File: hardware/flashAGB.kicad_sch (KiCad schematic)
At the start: 1 part

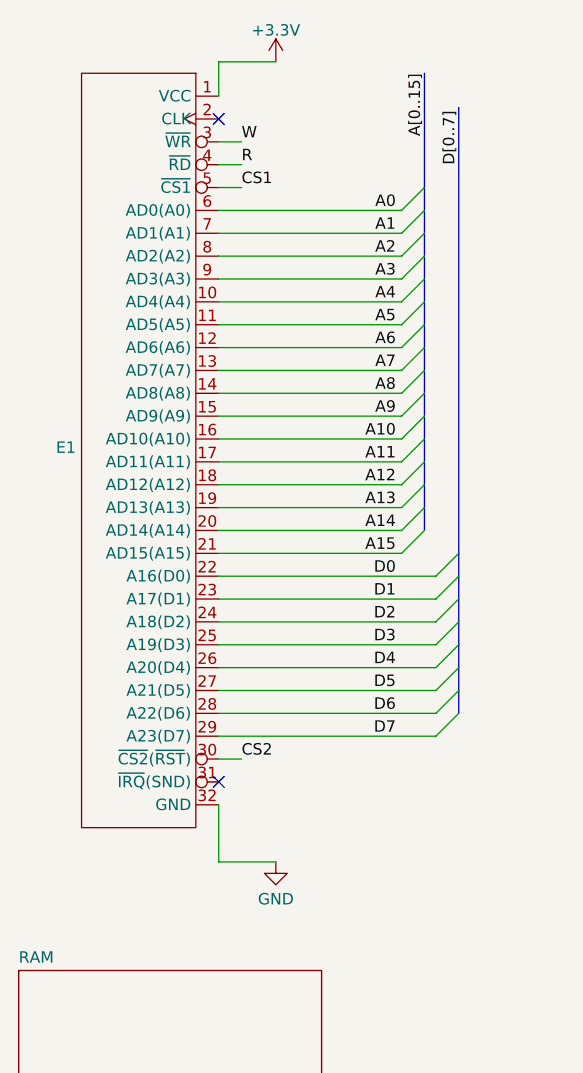
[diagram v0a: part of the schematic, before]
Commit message: Added feRAM
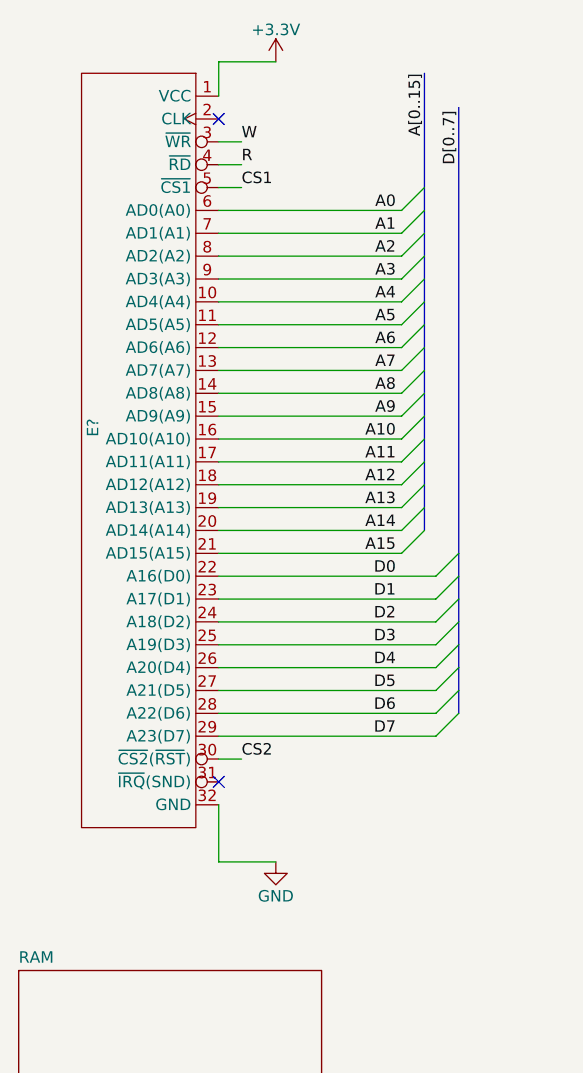
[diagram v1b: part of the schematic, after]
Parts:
- removed E1: ~, symbol AGB_cart:Cart
- added E?: ~, symbol AGB_common:Cart
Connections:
- net +3.3V: now also E?.1 (VCC)
- net A0: now also E?.6 (AD0(A0))
- net A1: now also E?.7 (AD1(A1))
- net A10: now also E?.16 (AD10(A10))
- net A11: now also E?.17 (AD11(A11))
- net A12: now also E?.18 (AD12(A12))
- net A13: now also E?.19 (AD13(A13))
- net A14: now also E?.20 (AD14(A14))
- net A15: now also E?.21 (AD15(A15))
- net A2: now also E?.8 (AD2(A2))
- net A3: now also E?.9 (AD3(A3))
- net A4: now also E?.10 (AD4(A4))
- net A5: now also E?.11 (AD5(A5))
- net A6: now also E?.12 (AD6(A6))
- net A7: now also E?.13 (AD7(A7))
- net A8: now also E?.14 (AD8(A8))
- net A9: now also E?.15 (AD9(A9))
- net CS1: now also E?.5 (~{CS1})
- net CS2: now also E?.30 (~{CS2}(~{RST}))
- net D0: now also E?.22 (A16(D0))
- net D1: now also E?.23 (A17(D1))
- net D2: now also E?.24 (A18(D2))
- net D3: now also E?.25 (A19(D3))
- net D4: now also E?.26 (A20(D4))
- net D5: now also E?.27 (A21(D5))
- net D6: now also E?.28 (A22(D6))
- net D7: now also E?.29 (A23(D7))
- net GND: now also E?.32 (GND)
- net R: now also E?.4 (~{RD})
- net W: now also E?.3 (~{WR})
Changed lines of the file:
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@@
   (symbol (lib_id "power:GND") (at 49.53 112.395 0) (mirror y) (unit 1)
     (in_bom yes) (on_board yes) (dnp no) (fields_autoplaced)
-    (property "Reference" "#PWR02" (at 49.53 118.745 0)
+    (property "Reference" "#PWR?" (at 49.53 118.745 0)
       (effects (font (size 1.27 1.27)) hide)
     )
-    (property "Value" "GND" (at 49.53 116.5305 0)
+    (property "Value" "GND" (at 49.53 116.205 0)
       (effects (font (size 1.27 1.27)))
     )
@@
       (project "flashAGB"
         (path "/b6299f43-2fc2-496b-b114-43ef73024503"
-          (reference "#PWR02") (unit 1)
+          (reference "#PWR?") (unit 1)
         )
       )
     )
   )
-  (symbol (lib_id "power:+3.3V") (at 49.53 23.495 0) (mirror y) (unit 1)
+  (symbol (lib_id "AGB_common:Cart") (at 30.48 64.135 270) (unit 1)
     (in_bom yes) (on_board yes) (dnp no) (fields_autoplaced)
-    (property "Reference" "#PWR01" (at 49.53 27.305 0)
-      (effects (font (size 1.27 1.27)) hide)
-    )
-    (property "Value" "+3.3V" (at 49.53 19.9931 0)
+    (property "Reference" "E?" (at 29.21 64.135 0)
       (effects (font (size 1.27 1.27)))
-    )
-    (property "Footprint" "" (at 49.53 23.495 0)
-      (effects (font (size 1.27 1.27)) hide)
-    )
-    (property "Datasheet" "" (at 49.53 23.495 0)
-      (effects (font (size 1.27 1.27)) hide)
-    )
-    (pin "1")
-    (instances
-      (project "flashAGB"
-        (path "/b6299f43-2fc2-496b-b114-43ef73024503"
-          (reference "#PWR01") (unit 1)
-        )
-      )
-    )
-  )
-  (symbol (lib_id "AGB_cart:Cart") (at 30.48 64.135 270) (unit 1)
-    (in_bom yes) (on_board yes) (dnp no)
-    (property "Reference" "E1" (at 27.305 66.3582 90)
-      (effects (font (size 1.27 1.27)) (justify right))
     )
     (property "Value" "~" (at 30.48 64.135 0)
@@
       (project "flashAGB"
         (path "/b6299f43-2fc2-496b-b114-43ef73024503"
-          (reference "E1") (unit 1)
+          (reference "E?") (unit 1)
         )
       )
+    )
+  )
+  (symbol (lib_id "power:+3.3V") (at 49.53 23.495 0) (mirror y) (unit 1)
+    (in_bom yes) (on_board yes) (dnp no) (fields_autoplaced)
+    (property "Reference" "#PWR?" (at 49.53 27.305 0)
+      (effects (font (size 1.27 1.27)) hide)
+    )
+    (property "Value" "+3.3V" (at 49.53 19.939 0)
+      (effects (font (size 1.27 1.27)))
+    )
+    (property "Footprint" "" (at 49.53 23.495 0)
+      (effects (font (size 1.27 1.27)) hide)
+    )
+    (property "Datasheet" "" (at 49.53 23.495 0)
+      (effects (font (size 1.27 1.27)) hide)
+    )
+    (pin "1")
+    (instances
+      (project "flashAGB"
+        (path "/b6299f43-2fc2-496b-b114-43ef73024503"
+          (reference "#PWR?") (unit 1)
+        )
+      )
